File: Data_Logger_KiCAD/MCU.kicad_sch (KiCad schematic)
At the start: 20 parts, among them J1 USB_C_Receptacle_USB2.0_16P, J2 Screw_Terminal_01x02, U2 ESP32-S3

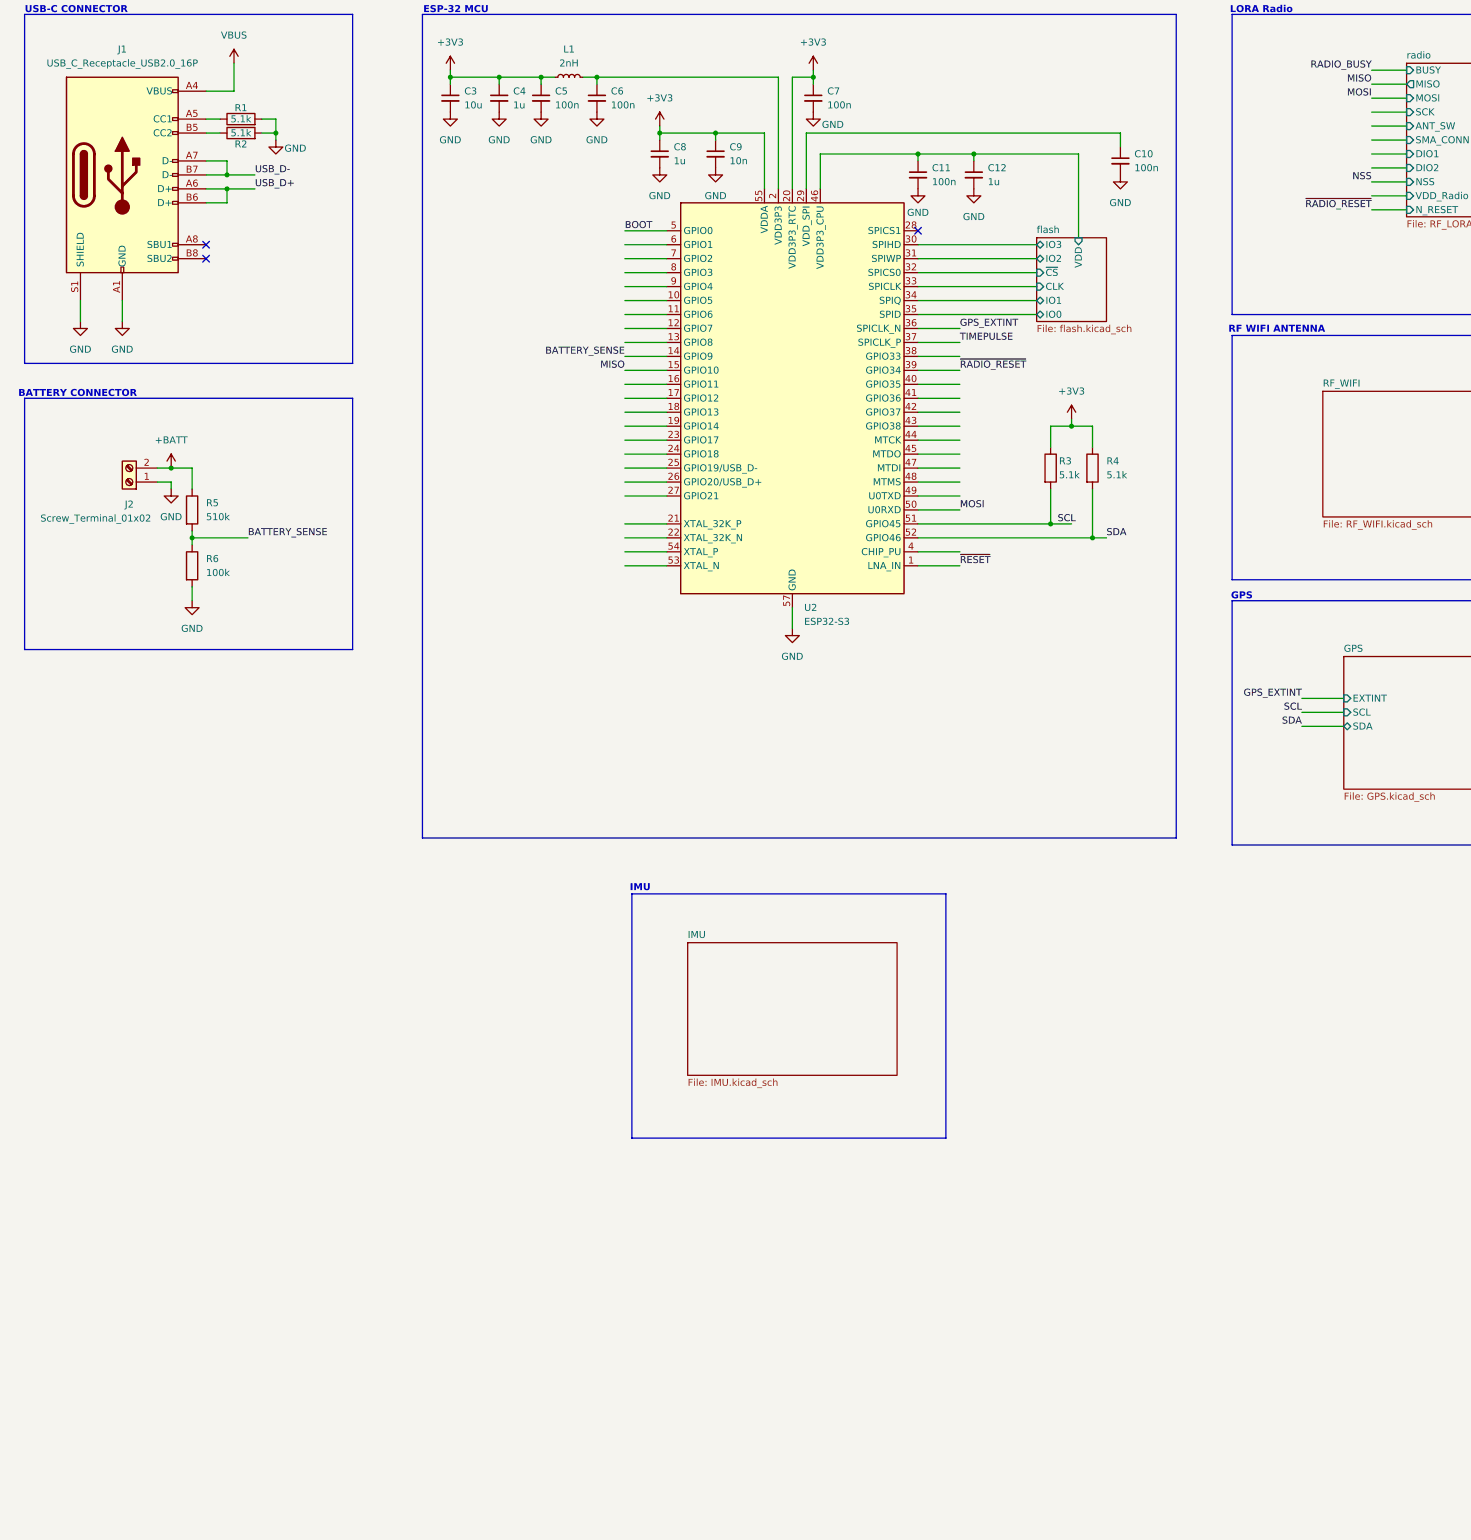
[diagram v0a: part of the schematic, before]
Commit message: add more I/O to MCU
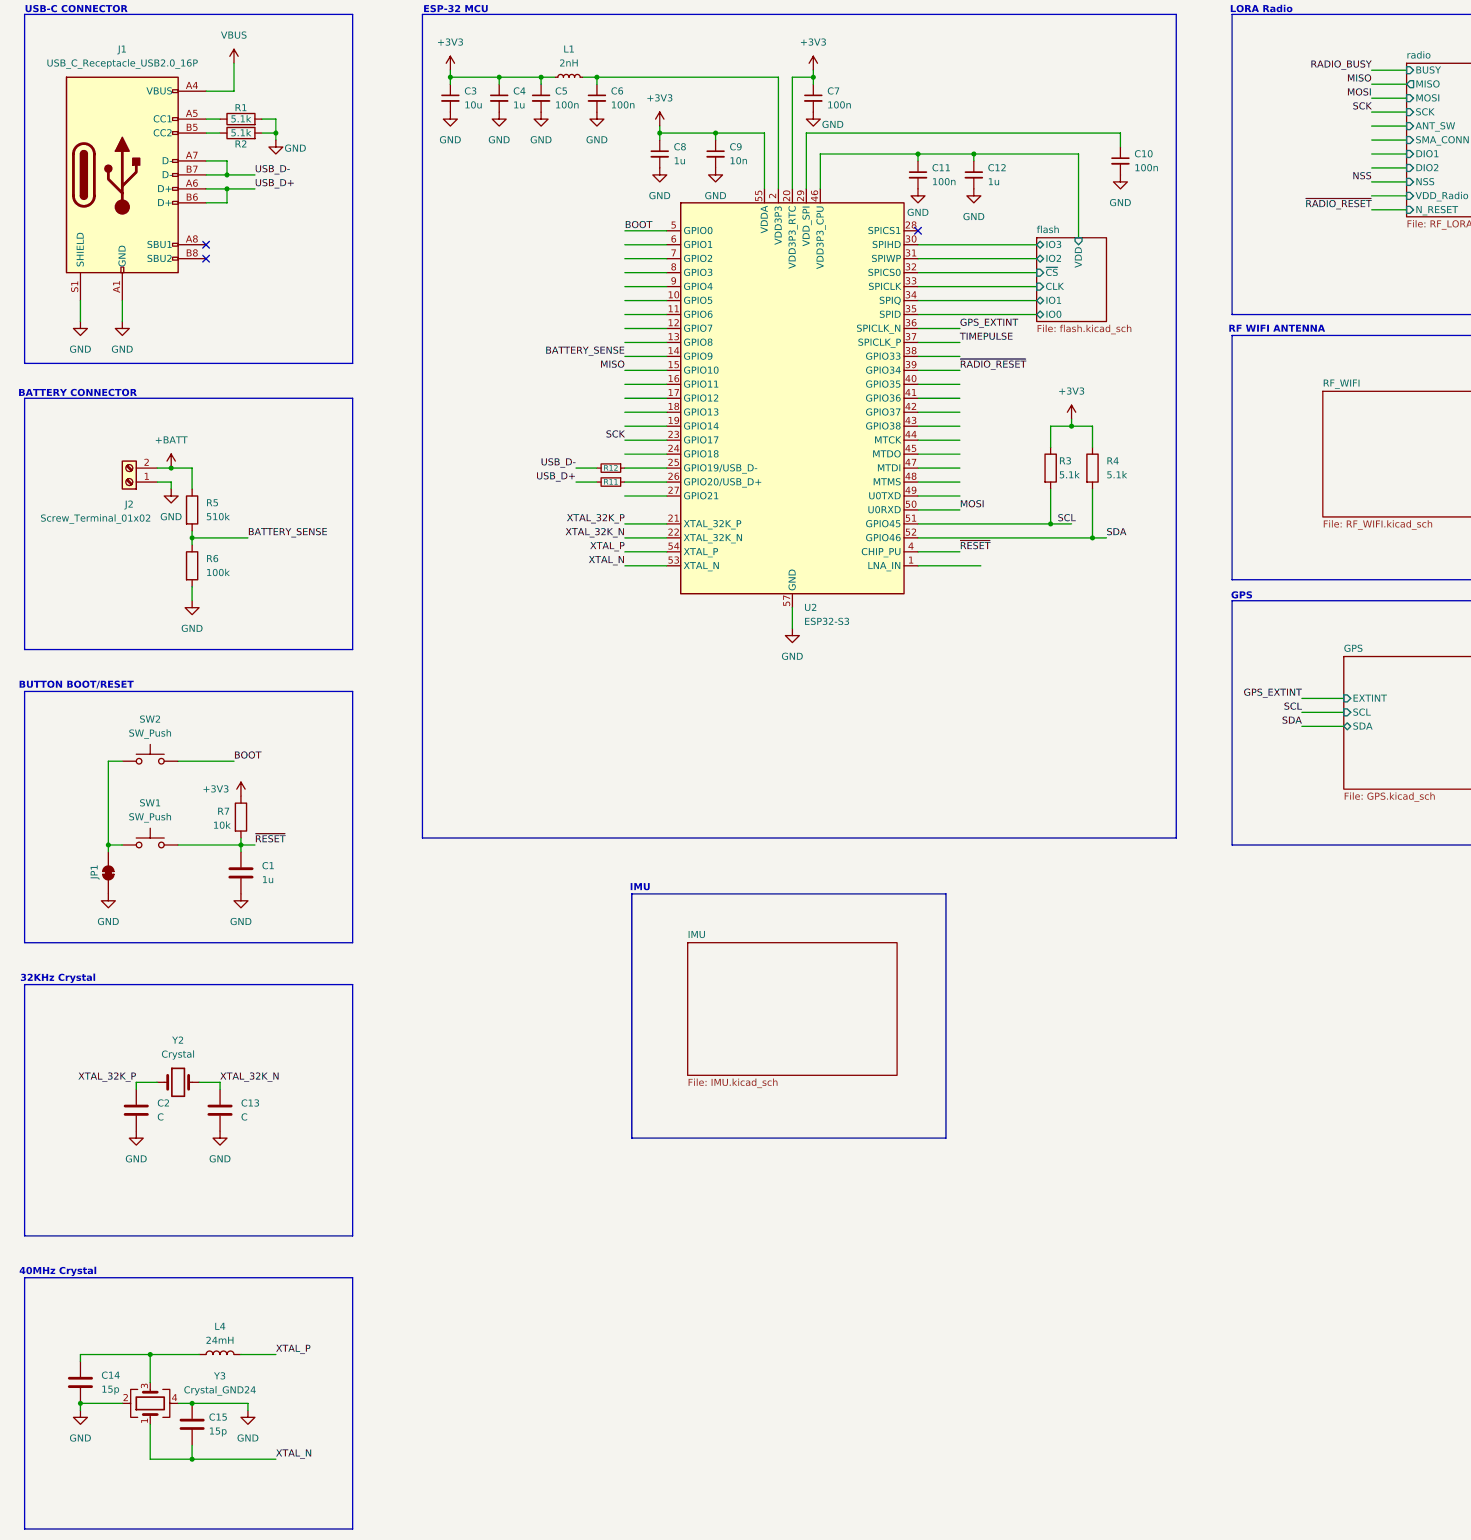
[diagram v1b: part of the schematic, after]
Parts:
- added C1: 1u, symbol Device:C
- added C13, C2: C, symbol Device:C
- added C14, C15: 15p, symbol Device:C
- added JP1: SolderJumper_2_Bridged, symbol Jumper:SolderJumper_2_Bridged
- added L4: 24mH, symbol Device:L
- added R11, R12: R_Small, symbol Device:R_Small
- added R7: 10k, symbol Device:R
- added SW1, SW2: SW_Push, symbol Switch:SW_Push
- added Y2: Crystal, symbol Device:Crystal
- added Y3: Crystal_GND24, symbol Device:Crystal_GND24
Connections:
- net +3V3: now also R7.1
- net BOOT: now also SW2.2
- net GND: now also C1.2, C13.2, C14.2, C15.1, C2.2, JP1.1 (A), Y3.2, Y3.4
- net USB_D+: now also R11.2
- net USB_D-: now also R12.2
- net ~{RESET}: now also U2.4 (CHIP_PU), C1.1, R7.2, SW1.2; no longer U2.1 (LNA_IN)
- net XTAL_32K_P: now reaches U2.21 (XTAL_32K_P)
- net XTAL_32K_P: now also C2.1, Y2.1
- net XTAL_32K_N: now reaches U2.22 (XTAL_32K_N)
- net XTAL_32K_N: now also C13.1, Y2.2
- net SCK: now reaches U2.23 (GPIO17)
- net at U2.25 (GPIO19/USB_D-): now also R12.1
- net at U2.26 (GPIO20/USB_D+): now also R11.1
- net XTAL_N: now reaches U2.53 (XTAL_N)
- net XTAL_N: now also C15.2, Y3.1
- net XTAL_P: now reaches U2.54 (XTAL_P)
- net XTAL_P: now also L4.2
- new net: JP1.2 (B), SW1.1, SW2.1
- new net: C14.1, L4.1, Y3.3
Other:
- note added: "32KHz Crystal"
- note added: "40MHz Crystal"
- note added: "BUTTON BOOT/RESET"

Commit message: update changes to MCU, add gitignore
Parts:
- added BZ1: Buzzer, symbol Device:Buzzer
- added D1: D_Small, symbol Device:D_Small
- added Q1: Q_NMOS_GSD, symbol Transistor_FET:Q_NMOS_GSD
- added R13: 10, symbol Device:R_Small
- added R14: 100k, symbol Device:R_Small
- L4: value 24mH -> 24nH
- R11, R12: value R_Small -> 0
- R5: value 510k -> 300k
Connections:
- net +3V3: now also BZ1.1 (+), D1.1 (K)
- net GND: now also Q1.2 (S), R14.2
- net USB_D+: now also R12.1; no longer R11.2
- net USB_D-: now also R11.2; no longer R12.2
- net at R11.1: now also U2.25 (GPIO19/USB_D-); no longer U2.26 (GPIO20/USB_D+)
- net BUZZER: now reaches U2.38 (GPIO33)
- net BUZZER: now also R13.1, R14.1
- new net: Q1.1 (G), R13.2
- new net: BZ1.2 (-), D1.2 (A), Q1.3 (D)
- new net: R12.2, U2.26 (GPIO20/USB_D+)
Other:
- note added: "8.4*(100k/100k+300k) = 2.1"

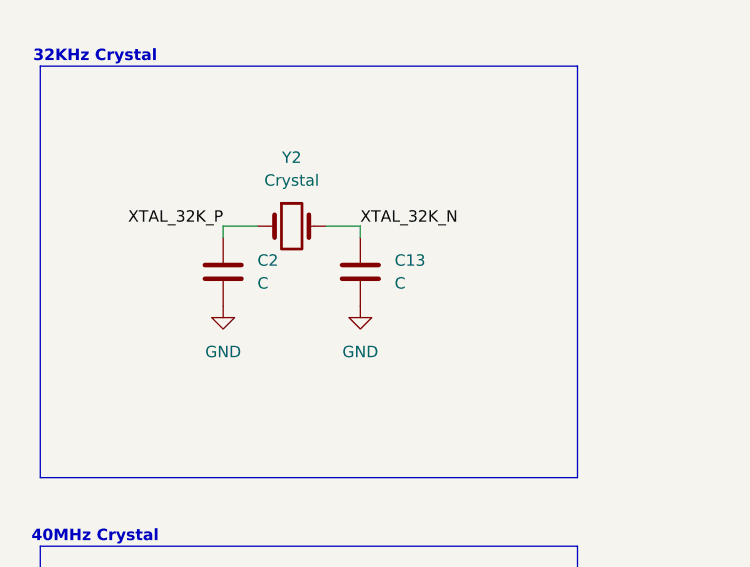
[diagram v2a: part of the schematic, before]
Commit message: add footprint/LCSC to parts
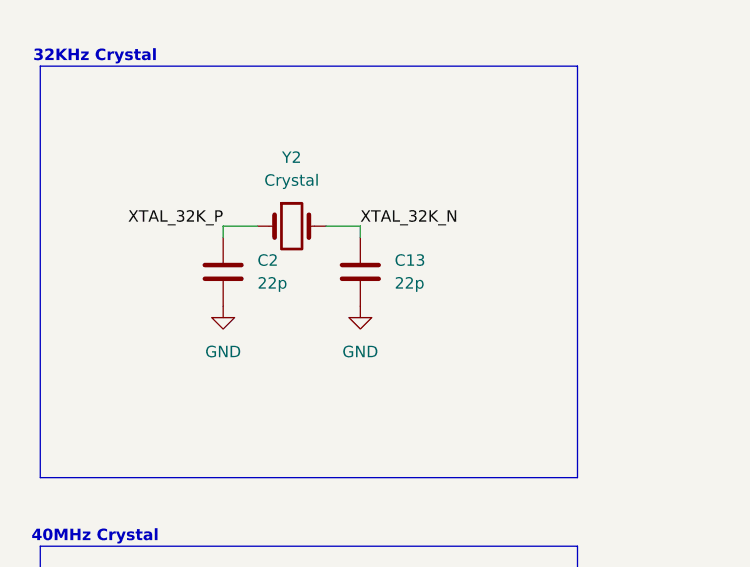
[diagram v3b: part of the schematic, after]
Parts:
- C1: footprint (none) -> Capacitor_SMD:C_0402_1005Metric; LCSC (none) -> C52923
- C13, C2: value C -> 22p; footprint (none) -> Capacitor_SMD:C_0402_1005Metric; LCSC (none) -> C1555
- C14, C15: footprint (none) -> Capacitor_SMD:C_0402_1005Metric; LCSC (none) -> C1548
- D1: footprint (none) -> Diode_SMD:D_SOD-123F; LCSC (none) -> C64898
- J1: footprint (none) -> Connector_USB:USB_C_Receptacle_G-Switch_GT-USB-7010ASV; LCSC (none) -> C2988369
- J2: footprint (none) -> TerminalBlock:TerminalBlock_Xinya_XY308-2.54-2P_1x02_P2.54mm_Horizontal
- JP1: footprint (none) -> Jumper:SolderJumper-2_P1.3mm_Bridged_RoundedPad1.0x1.5mm
- L4: footprint (none) -> Inductor_SMD:L_0402_1005Metric; LCSC (none) -> C74301
- Q1: footprint (none) -> Package_TO_SOT_SMD:SOT-23; LCSC (none) -> C28646273
- R1, R2, R3, R4: LCSC (none) -> C25905
- R13: LCSC (none) -> C25077
- R14, R6: LCSC (none) -> C25741
- R5: LCSC (none) -> C25774
- R7: LCSC (none) -> C25744
- SW1, SW2: footprint (none) -> Button_Switch_SMD:SW_SPST_PTS810
- Y3: footprint (none) -> Crystal:Crystal_SMD_2016-4Pin_2.0x1.6mm; LCSC (none) -> C501798
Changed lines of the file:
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@@
 			)
 		)
-		(property "Value" "C"
+		(property "Value" "22p"
 			(at 46.99 253.9999 0)
 			(effects
@@
 			)
 		)
-		(property "Footprint" ""
+		(property "Footprint" "Capacitor_SMD:C_0402_1005Metric"
 			(at 44.1452 256.54 0)
 			(effects
@@
 			)
 		)
+		(property "LCSC" "C1555"
+			(at 43.18 252.73 0)
+			(effects
+				(font
+					(size 1.27 1.27)
+				)
+				(hide yes)
+			)
+		)
 		(pin "2"
 		)
@@
 			)
 		)
-		(property "Footprint" ""
+		(property "Footprint" "Jumper:SolderJumper-2_P1.3mm_Bridged_RoundedPad1.0x1.5mm"
 			(at 38.1 209.55 0)
 			(effects
@@
 			)
 		)
+		(property "LCSC" ""
+			(at 38.1 209.55 0)
+			(effects
+				(font
+					(size 1.27 1.27)
+				)
+				(hide yes)
+			)
+		)
 		(pin "2"
 		)
@@
 			)
 		)
+		(property "LCSC" "C25905"
+			(at 209.55 135.89 0)
+			(effects
+				(font
+					(size 1.27 1.27)
+				)
+				(hide yes)
+			)
+		)
 		(pin "2"
 		)
@@
 			)
 		)
-		(property "Footprint" ""
+		(property "Footprint" "Package_TO_SOT_SMD:SOT-23"
 			(at 59.69 359.41 0)
 			(effects
@@
 			)
 		)
+		(property "LCSC" "C28646273"
+			(at 54.61 361.95 0)
+			(effects
+				(font
+					(size 1.27 1.27)
+				)
+				(hide yes)
+			)
+		)
 		(pin "1"
 		)
@@
 			)
 		)
+		(property "LCSC" "C25744"
+			(at 62.23 199.39 0)
+			(effects
+				(font
+					(size 1.27 1.27)
+				)
+				(hide yes)
+			)
+		)
 		(pin "1"
 		)
@@
 			)
 		)
-		(property "Footprint" ""
+		(property "Footprint" "Crystal:Crystal_SMD_2016-4Pin_2.0x1.6mm"
 			(at 45.72 306.07 0)
 			(effects
@@
 			)
 		)
+		(property "LCSC" "C501798"
+			(at 45.72 306.07 0)
+			(effects
+				(font
+					(size 1.27 1.27)
+				)
+				(hide yes)
+			)
+		)
 		(pin "3"
 		)
@@
 			)
 		)
-		(property "Footprint" ""
+		(property "Footprint" "Capacitor_SMD:C_0402_1005Metric"
 			(at 54.3052 313.69 0)
 			(effects
@@
 			)
 		)
+		(property "LCSC" "C1548"
+			(at 53.34 309.88 0)
+			(effects
+				(font
+					(size 1.27 1.27)
+				)
+				(hide yes)
+			)
+		)
 		(pin "1"
 		)
@@
 			)
 		)
-		(property "Footprint" ""
+		(property "Footprint" "TerminalBlock:TerminalBlock_Xinya_XY308-2.54-2P_1x02_P2.54mm_Horizontal"
 			(at 41.91 138.43 0)
 			(effects
@@
 			)
 		)
+		(property "LCSC" ""
+			(at 41.91 138.43 0)
+			(effects
+				(font
+					(size 1.27 1.27)
+				)
+				(hide yes)
+			)
+		)
 		(pin "2"
 		)
@@
 			)
 		)
+		(property "LCSC" "C25905"
+			(at 62.23 72.39 90)
+			(effects
+				(font
+					(size 1.27 1.27)
+				)
+				(hide yes)
+			)
+		)
 		(pin "2"
 		)
@@
 			)
 		)
-		(property "Footprint" ""
+		(property "Footprint" "Button_Switch_SMD:SW_SPST_PTS810"
 			(at 45.72 199.39 0)
 			(effects
@@
 			)
 		)
+		(property "LCSC" ""
+			(at 45.72 204.47 0)
+			(effects
+				(font
+					(size 1.27 1.27)
+				)
+				(hide yes)
+			)
+		)
 		(pin "1"
 		)
@@
 			)
 		)
+		(property "LCSC" "C25905"
+			(at 62.23 74.93 90)
+			(effects
+				(font
+					(size 1.27 1.27)
+				)
+				(hide yes)
+			)
+		)
 		(pin "1"
 		)
@@
 			)
 		)
-		(property "Footprint" ""
+		(property "Footprint" "Capacitor_SMD:C_0402_1005Metric"
 			(at 33.9852 306.07 0)
 			(effects
@@
 			)
 		)
+		(property "LCSC" "C1548"
+			(at 33.02 302.26 0)
+			(effects
+				(font
+					(size 1.27 1.27)
+				)
+				(hide yes)
+			)
+		)
 		(pin "1"
 		)
@@
 			)
 		)
-		(property "Footprint" ""
+		(property "Footprint" "Connector_USB:USB_C_Receptacle_G-Switch_GT-USB-7010ASV"
 			(at 44.45 82.55 0)
 			(effects
@@
 			)
 		)
+		(property "LCSC" "C2988369"
+			(at 40.64 82.55 0)
+			(effects
+				(font
+					(size 1.27 1.27)
+				)
+				(hide yes)
+			)
+		)
 		(pin "S1"
 		)
@@
 			)
 		)
+		(property "LCSC" "C25774"
+			(at 53.34 143.51 0)
+			(effects
+				(font
+					(size 1.27 1.27)
+				)
+				(hide yes)
+			)
+		)
 		(pin "1"
 		)
@@
 			)
 		)
-		(property "Value" "C"
+		(property "Value" "22p"
 			(at 62.23 253.9999 0)
 			(effects
@@
 			)
 		)
-		(property "Footprint" ""
+		(property "Footprint" "Capacitor_SMD:C_0402_1005Metric"
 			(at 59.3852 256.54 0)
 			(effects
@@
 			)
 		)
+		(property "LCSC" "C1555"
+			(at 58.42 252.73 0)
+			(effects
+				(font
+					(size 1.27 1.27)
+				)
+				(hide yes)
+			)
+		)
 		(pin "2"
 		)
@@
 			)
 		)
-		(property "Footprint" ""
+		(property "Footprint" "Inductor_SMD:L_0402_1005Metric"
 			(at 58.42 297.18 0)
 			(effects
@@
 			)
 		)
+		(property "LCSC" "C74301"
+			(at 58.42 297.18 0)
+			(effects
+				(font
+					(size 1.27 1.27)
+				)
+				(hide yes)
+			)
+		)
 		(pin "2"
 		)
@@
 			)
 		)
-		(property "Footprint" ""
+		(property "Footprint" "Capacitor_SMD:C_0402_1005Metric"
 			(at 63.1952 213.36 0)
 			(effects
@@
 			)
 		)
+		(property "LCSC" "C52923"
+			(at 62.23 209.55 0)
+			(effects
+				(font
+					(size 1.27 1.27)
+				)
+				(hide yes)
+			)
+		)
 		(pin "2"
 		)
@@
 			)
 		)
+		(property "LCSC" "C25741"
+			(at 41.91 365.76 0)
+			(effects
+				(font
+					(size 1.27 1.27)
+				)
+				(hide yes)
+			)
+		)
 		(pin "1"
 		)
@@
 			)
 		)
+		(property "LCSC" "C25077"
+			(at 44.45 361.95 90)
+			(effects
+				(font
+					(size 1.27 1.27)
+				)
+				(hide yes)
+			)
+		)
 		(pin "2"
 		)
@@
 			)
 		)
-		(property "Footprint" ""
+		(property "Footprint" "Button_Switch_SMD:SW_SPST_PTS810"
 			(at 45.72 184.15 0)
 			(effects
@@
 			)
 		)
+		(property "LCSC" ""
+			(at 45.72 189.23 0)
+			(effects
+				(font
+					(size 1.27 1.27)
+				)
+				(hide yes)
+			)
+		)
 		(pin "1"
 		)
@@
 			)
 		)
+		(property "LCSC" "C25741"
+			(at 53.34 153.67 0)
+			(effects
+				(font
+					(size 1.27 1.27)
+				)
+				(hide yes)
+			)
+		)
 		(pin "2"
 		)
@@
 			)
 		)
+		(property "LCSC" "C25905"
+			(at 217.17 135.89 0)
+			(effects
+				(font
+					(size 1.27 1.27)
+				)
+				(hide yes)
+			)
+		)
 		(pin "2"
 		)
@@
 			)
 		)
-		(property "Footprint" ""
+		(property "Footprint" "Diode_SMD:D_SOD-123F"
 			(at 57.15 351.79 90)
 			(effects
@@
 			(at 57.15 351.79 0)
 			(effects
+				(font
+					(size 1.27 1.27)
+				)
+				(hide yes)
+			)
+		)
+		(property "LCSC" "C64898"
+			(at 57.15 351.79 0)
+			(effects
